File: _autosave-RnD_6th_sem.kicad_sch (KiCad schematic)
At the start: 47 parts, among them J1 HVDC1, J2 PWM, J3 HVDC2, Q1 IGLD60R190D1, Q2 IGLD60R190D1, U1 2EDF7275K

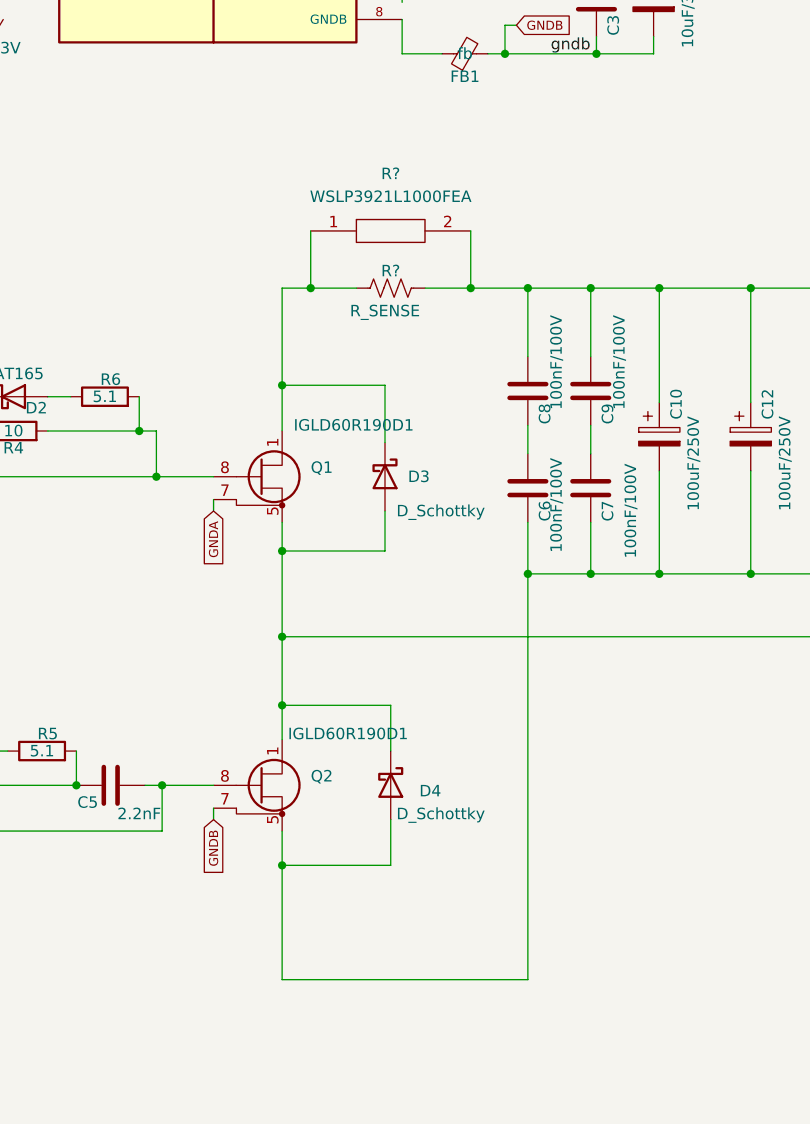
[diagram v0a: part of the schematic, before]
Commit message: added current sense resistors
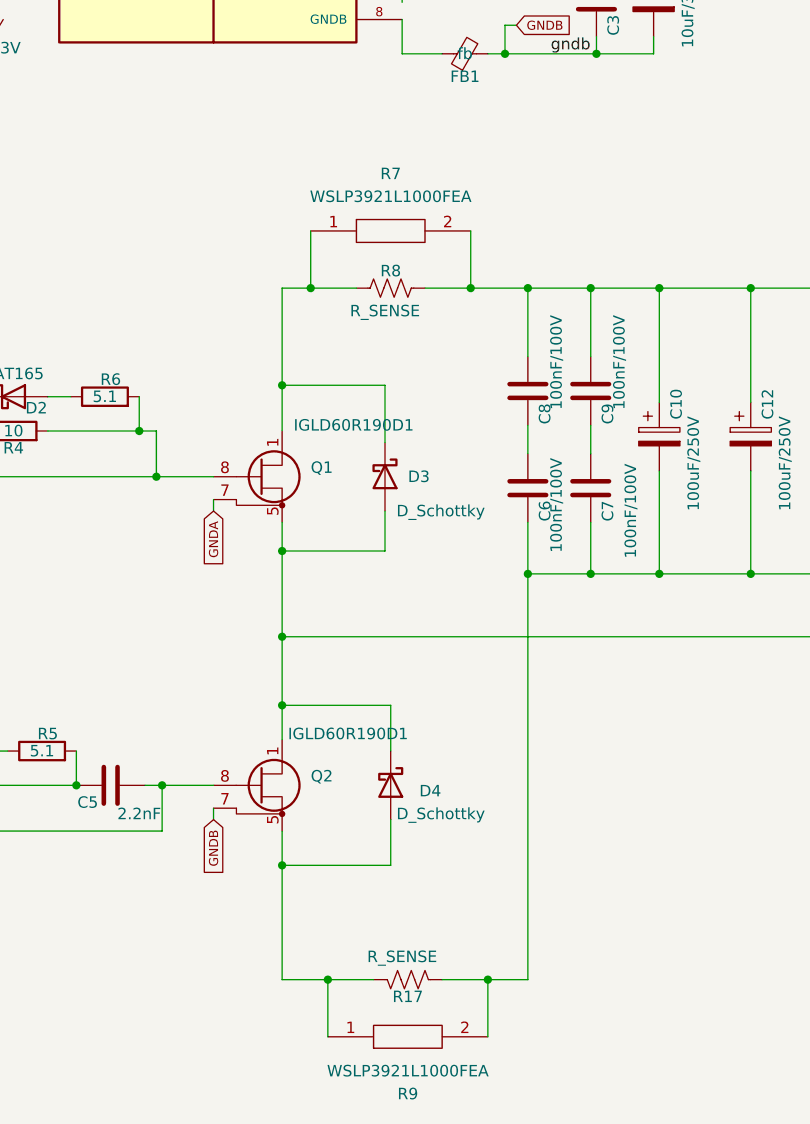
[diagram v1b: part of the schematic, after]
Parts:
- added R17: R_SENSE, symbol Device:R_US
- added R9: WSLP3921L1000FEA, footprint:RESC10052X50N, symbol WSLP3921L1000FEA:WSLP3921L1000FEA
- C10, C12, C15, C16: footprint (none) -> Capacitor_SMD:CP_Elec_4x5.8
- R7: renamed from R?; footprint RESC10052X50N -> footprint:RESC10052X50N
- gave numbers to parts that had none: 1
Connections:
- net at C10.2, C12.2, C6.1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: now also R17.2, R9.2; no longer D4.2 (A), Q2.5 (S), Q2.6 (S), Q2.9 (S)
- new net: D4.2 (A), Q2.5 (S), Q2.6 (S), Q2.9 (S), R17.1, R9.1
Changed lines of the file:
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@@
   (junction (at 41.275 42.545) (diameter 0) (color 0 0 0 0)
   )
+  (junction (at 153.035 149.86) (diameter 0) (color 0 0 0 0)
+  )
   (junction (at 200.025 73.025) (diameter 0) (color 0 0 0 0)
   )
@@
   )
   (junction (at 180.34 20.32) (diameter 0) (color 0 0 0 0)
+  )
+  (junction (at 170.815 149.86) (diameter 0) (color 0 0 0 0)
   )
   (junction (at 182.245 73.025) (diameter 0) (color 0 0 0 0)
@@
     (stroke (width 0) (type default) (color 0 0 0 0))
   )
+  (wire (pts (xy 170.815 149.86) (xy 165.735 149.86))
+    (stroke (width 0) (type default) (color 0 0 0 0))
+  )
   (wire (pts (xy 28.575 23.495) (xy 32.385 23.495))
     (stroke (width 0) (type default) (color 0 0 0 0))
@@
     (stroke (width 0) (type default) (color 0 0 0 0))
   )
+  (wire (pts (xy 170.815 156.21) (xy 170.815 149.86))
+    (stroke (width 0) (type default) (color 0 0 0 0))
+  )
   (wire (pts (xy 134.62 128.27) (xy 140.335 128.27))
     (stroke (width 0) (type default) (color 0 0 0 0))
@@
     (stroke (width 0) (type default) (color 0 0 0 0))
   )
-  (wire (pts (xy 147.955 149.86) (xy 175.26 149.86))
+  (wire (pts (xy 147.955 149.86) (xy 153.035 149.86))
     (stroke (width 0) (type default) (color 0 0 0 0))
   )
@@
     (stroke (width 0) (type default) (color 0 0 0 0))
   )
+  (wire (pts (xy 153.035 156.21) (xy 153.035 149.86))
+    (stroke (width 0) (type default) (color 0 0 0 0))
+  )
   (wire (pts (xy 104.14 133.35) (xy 104.14 128.27))
     (stroke (width 0) (type default) (color 0 0 0 0))
@@
     (stroke (width 0) (type default) (color 0 0 0 0))
   )
+  (wire (pts (xy 153.035 149.86) (xy 158.115 149.86))
+    (stroke (width 0) (type default) (color 0 0 0 0))
+  )
   (wire (pts (xy 175.26 80.645) (xy 175.26 73.025))
     (stroke (width 0) (type default) (color 0 0 0 0))
@@
   )
   (wire (pts (xy 95.25 40.005) (xy 116.205 40.005))
+    (stroke (width 0) (type default) (color 0 0 0 0))
+  )
+  (wire (pts (xy 170.815 149.86) (xy 175.26 149.86))
     (stroke (width 0) (type default) (color 0 0 0 0))
   )
@@
       (effects (font (size 1.27 1.27)) (justify left))
     )
-    (property "Footprint" "" (id 2) (at 190.8302 93.345 0)
+    (property "Footprint" "Capacitor_SMD:CP_Elec_4x5.8" (id 2) (at 190.8302 93.345 0)
       (effects (font (size 1.27 1.27)) hide)
     )
@@
       (effects (font (size 1.27 1.27)) (justify left))
     )
-    (property "Footprint" "" (id 2) (at 190.1952 45.085 0)
+    (property "Footprint" "Capacitor_SMD:CP_Elec_4x5.8" (id 2) (at 190.1952 45.085 0)
       (effects (font (size 1.27 1.27)) hide)
     )
     (property "Datasheet" "~" (id 3) (at 189.23 41.275 0)
+      (effects (font (size 1.27 1.27)) hide)
+    )
+    (pin "1")
+    (pin "2")
+  )
+  (symbol (lib_id "Device:R_US") (at 161.925 149.86 90) (mirror x) (unit 1)
+    (in_bom yes) (on_board yes)
+    (property "Reference" "R17" (id 0) (at 161.925 151.765 90))
+    (property "Value" "R_SENSE" (id 1) (at 161.29 147.32 90))
+    (property "Footprint" "" (id 2) (at 162.179 150.876 90)
+      (effects (font (size 1.27 1.27)) hide)
+    )
+    (property "Datasheet" "~" (id 3) (at 161.925 149.86 0)
       (effects (font (size 1.27 1.27)) hide)
     )
@@
     (property "Datasheet" "~" (id 3) (at 168.275 46.99 0)
       (effects (font (size 1.27 1.27)) hide)
+    )
+    (pin "1")
+    (pin "2")
+  )
+  (symbol (lib_id "WSLP3921L1000FEA:WSLP3921L1000FEA") (at 153.035 156.21 0) (mirror x) (unit 1)
+    (in_bom yes) (on_board yes) (fields_autoplaced)
+    (property "Reference" "R9" (id 0) (at 161.925 162.56 0))
+    (property "Value" "WSLP3921L1000FEA" (id 1) (at 161.925 160.02 0))
+    (property "Footprint" "footprint:RESC10052X50N" (id 2) (at 167.005 157.48 0)
+      (effects (font (size 1.27 1.27)) (justify left) hide)
+    )
+    (property "Datasheet" "https://datasheet.datasheetarchive.com/originals/distributors/Datasheets_SAMA/cd369b67f640568f5c60fc944b86acf3.pdf" (id 3) (at 167.005 154.94 0)
+      (effects (font (size 1.27 1.27)) (justify left) hide)
+    )
+    (property "Description" "Current Sense Resistors - SMD 9W 0.0001ohm 1%" (id 4) (at 167.005 152.4 0)
+      (effects (font (size 1.27 1.27)) (justify left) hide)
+    )
+    (property "Height" "0.5" (id 5) (at 167.005 149.86 0)
+      (effects (font (size 1.27 1.27)) (justify left) hide)
+    )
+    (property "Manufacturer_Name" "Vishay" (id 6) (at 167.005 147.32 0)
+      (effects (font (size 1.27 1.27)) (justify left) hide)
+    )
+    (property "Manufacturer_Part_Number" "WSLP3921L1000FEA" (id 7) (at 167.005 144.78 0)
+      (effects (font (size 1.27 1.27)) (justify left) hide)
+    )
+    (property "Mouser Part Number" "71-WSLP3921L1000FEA" (id 8) (at 167.005 142.24 0)
+      (effects (font (size 1.27 1.27)) (justify left) hide)
+    )
+    (property "Mouser Price/Stock" "https://www.mouser.co.uk/ProductDetail/Vishay-Dale/WSLP3921L1000FEA?qs=TiOZkKH1s2S5b3T%252BuIp%2FVQ%3D%3D" (id 9) (at 167.005 139.7 0)
+      (effects (font (size 1.27 1.27)) (justify left) hide)
+    )
+    (property "Arrow Part Number" "" (id 10) (at 167.005 137.16 0)
+      (effects (font (size 1.27 1.27)) (justify left) hide)
+    )
+    (property "Arrow Price/Stock" "" (id 11) (at 167.005 134.62 0)
+      (effects (font (size 1.27 1.27)) (justify left) hide)
+    )
+    (property "Mouser Testing Part Number" "" (id 12) (at 167.005 132.08 0)
+      (effects (font (size 1.27 1.27)) (justify left) hide)
+    )
+    (property "Mouser Testing Price/Stock" "" (id 13) (at 167.005 129.54 0)
+      (effects (font (size 1.27 1.27)) (justify left) hide)
     )
     (pin "1")
@@
   (symbol (lib_id "WSLP3921L1000FEA:WSLP3921L1000FEA") (at 151.13 66.675 0) (unit 1)
     (in_bom yes) (on_board yes) (fields_autoplaced)
-    (property "Reference" "R?" (id 0) (at 160.02 60.325 0))
+    (property "Reference" "R7" (id 0) (at 160.02 60.325 0))
     (property "Value" "WSLP3921L1000FEA" (id 1) (at 160.02 62.865 0))
-    (property "Footprint" "RESC10052X50N" (id 2) (at 165.1 65.405 0)
+    (property "Footprint" "footprint:RESC10052X50N" (id 2) (at 165.1 65.405 0)
       (effects (font (size 1.27 1.27)) (justify left) hide)
     )
@@
   (symbol (lib_id "Device:R_US") (at 160.02 73.025 90) (unit 1)
     (in_bom yes) (on_board yes)
-    (property "Reference" "R?" (id 0) (at 160.02 71.12 90))
+    (property "Reference" "R8" (id 0) (at 160.02 71.12 90))
     (property "Value" "R_SENSE" (id 1) (at 159.385 75.565 90))
     (property "Footprint" "" (id 2) (at 160.274 72.009 90)
@@
       (effects (font (size 1.27 1.27)) (justify left))
     )
-    (property "Footprint" "" (id 2) (at 188.2902 29.845 0)
+    (property "Footprint" "Capacitor_SMD:CP_Elec_4x5.8" (id 2) (at 188.2902 29.845 0)
       (effects (font (size 1.27 1.27)) hide)
     )
@@
       (effects (font (size 1.27 1.27)) (justify left))
     )
-    (property "Footprint" "" (id 2) (at 200.9902 93.345 0)
+    (property "Footprint" "Capacitor_SMD:CP_Elec_4x5.8" (id 2) (at 200.9902 93.345 0)
       (effects (font (size 1.27 1.27)) hide)
     )
@@
     )
     (path "/4cdaf42b-87c1-4a9f-ada9-ae3a181df2b5"
-      (reference "C10") (unit 1) (value "100uF/250V") (footprint "")
+      (reference "C10") (unit 1) (value "100uF/250V") (footprint "Capacitor_SMD:CP_Elec_4x5.8")
     )
     (path "/e7e095f7-9599-4228-a12f-4840d99fda6f"
-      (reference "C12") (unit 1) (value "100uF/250V") (footprint "")
+      (reference "C12") (unit 1) (value "100uF/250V") (footprint "Capacitor_SMD:CP_Elec_4x5.8")
     )
     (path "/59eecde8-bb78-4d2f-a2d2-80e0155e7906"
@@
     )
     (path "/d32f603e-9542-4ef6-8c14-612e3a1db959"
-      (reference "C15") (unit 1) (value "10uF/35V") (footprint "")
+      (reference "C15") (unit 1) (value "10uF/35V") (footprint "Capacitor_SMD:CP_Elec_4x5.8")
     )
     (path "/7473794a-112e-4a68-9c19-a0ecda281169"
-      (reference "C16") (unit 1) (value "10uF/35V") (footprint "")
+      (reference "C16") (unit 1) (value "10uF/35V") (footprint "Capacitor_SMD:CP_Elec_4x5.8")
     )
     (path "/d40d8f52-3514-4cd0-abf2-16883ea85ff3"
@@
       (reference "R6") (unit 1) (value "5.1") (footprint "Resistor_SMD:R_0805_2012Metric")
     )
+    (path "/9af475f9-9a4a-4b1e-bc9e-6a5160d800cd"
+      (reference "R7") (unit 1) (value "WSLP3921L1000FEA") (footprint "footprint:RESC10052X50N")
+    )
+    (path "/cac2ebfd-9af4-4186-a729-3c25d7ec672e"
+      (reference "R8") (unit 1) (value "R_SENSE") (footprint "")
+    )
+    (path "/8ab46d10-f250-46a4-ab4f-73b7a7aef8c7"
+      (reference "R9") (unit 1) (value "WSLP3921L1000FEA") (footprint "footprint:RESC10052X50N")
+    )
     (path "/8d110906-4741-433a-afce-fcafbc601664"
       (reference "R10") (unit 1) (value "4.7k") (footprint "Resistor_SMD:R_0805_2012Metric")
@@
       (reference "R16") (unit 1) (value "10k") (footprint "Resistor_SMD:R_0805_2012Metric")
     )
-    (path "/9af475f9-9a4a-4b1e-bc9e-6a5160d800cd"
-      (reference "R?") (unit 1) (value "WSLP3921L1000FEA") (footprint "RESC10052X50N")
-    )
-    (path "/cac2ebfd-9af4-4186-a729-3c25d7ec672e"
-      (reference "R?") (unit 1) (value "R_SENSE") (footprint "")
+    (path "/7a4ba221-1368-4659-b0d7-a1d3db38b450"
+      (reference "R17") (unit 1) (value "R_SENSE") (footprint "")
     )
     (path "/929a0c5a-85ce-4abc-b13f-988818069efe"
